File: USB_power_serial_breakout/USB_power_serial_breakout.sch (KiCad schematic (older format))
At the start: 18 parts, among them J1 Mount2, J2 Mount2, J3 USB_B, J4 UART, U1 FT230XS

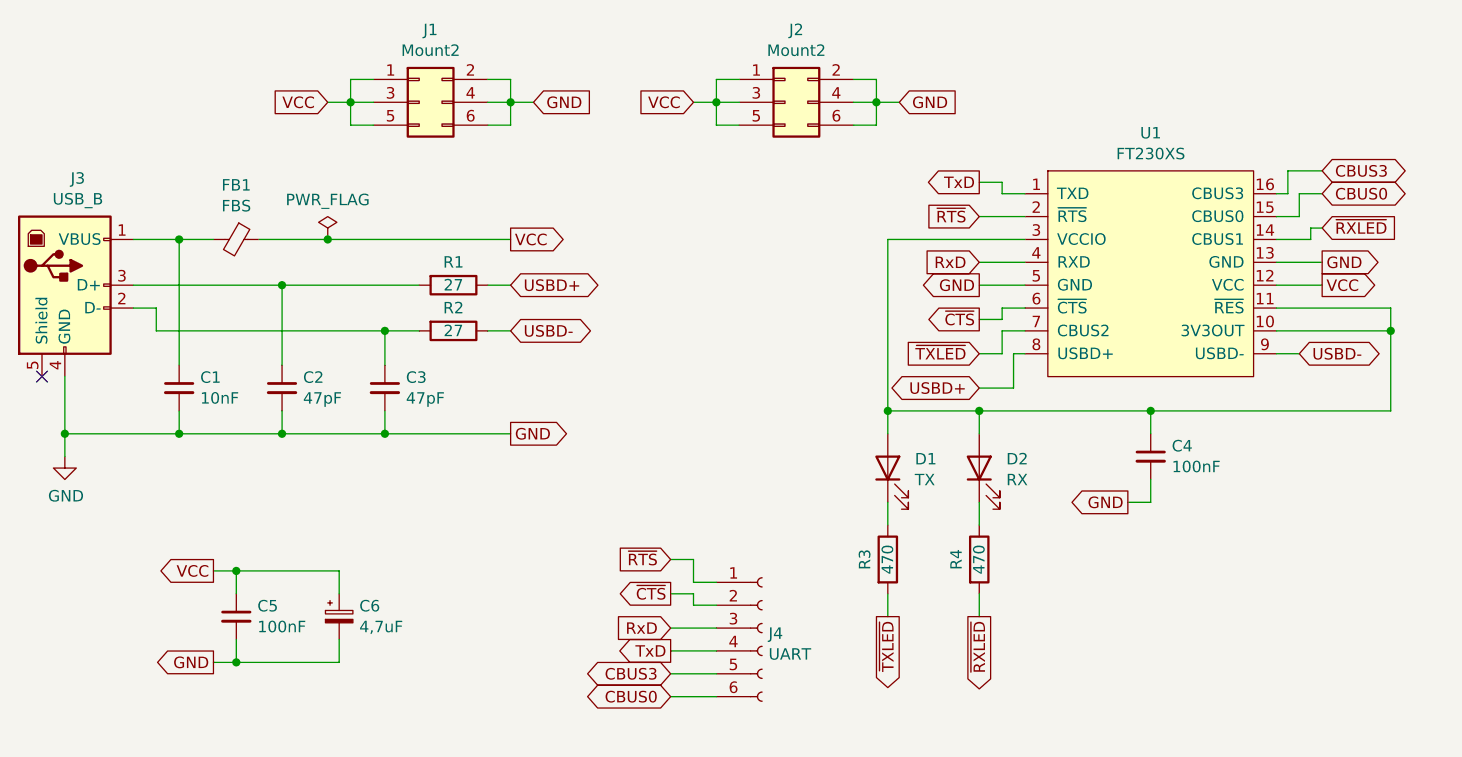
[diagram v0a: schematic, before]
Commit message: Updated the USB breakout board
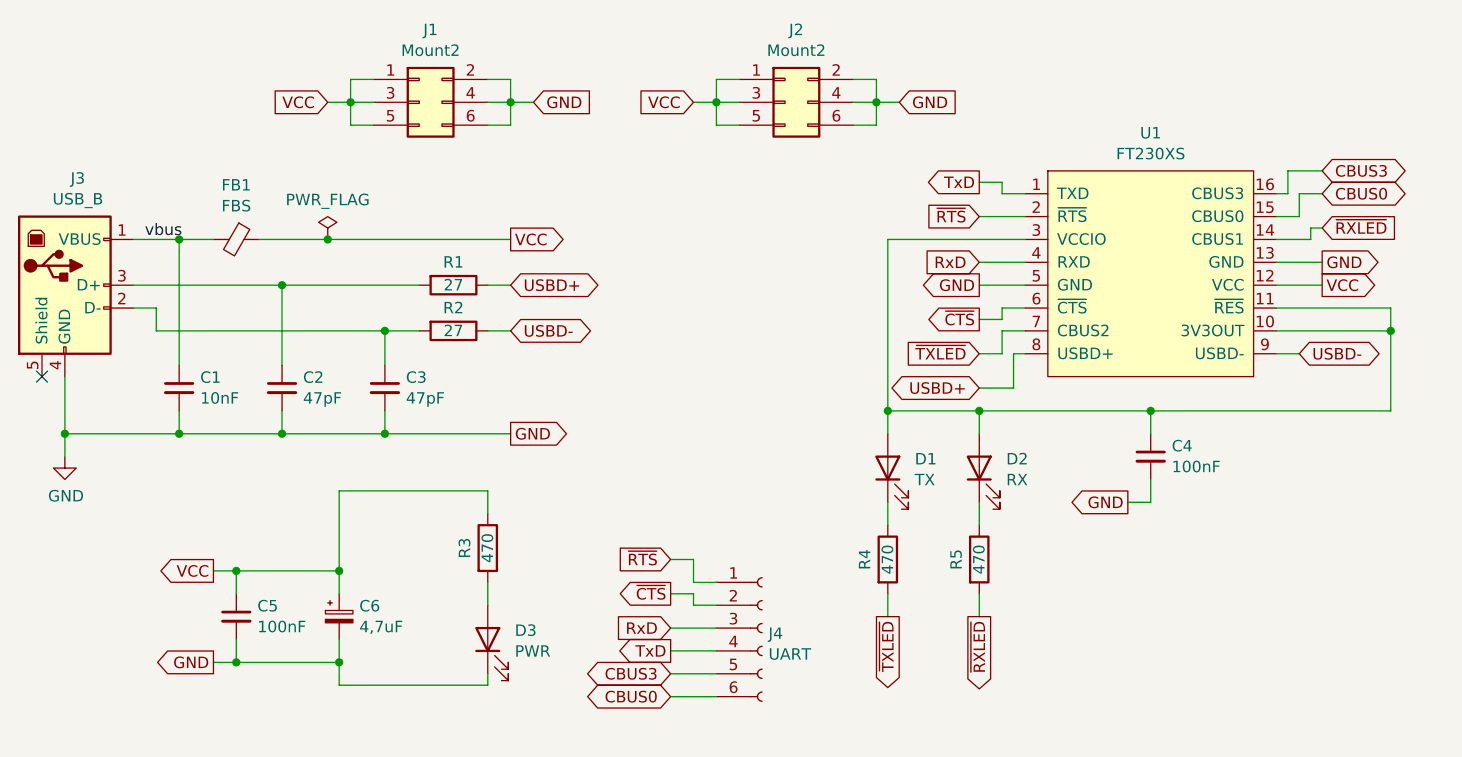
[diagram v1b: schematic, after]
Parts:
- added D3: PWR, LED_THT:LED_D3.0mm, symbol Device:LED
- added R3: 470, Resistor_SMD:R_1206_3216Metric_Pad1.30x1.75mm_HandSolder, symbol Device:R
- renumbered R3 to R4, R4 to R5
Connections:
- net GND: now also D3.1 (K)
- net VCC: now also R3.1
- net vbus: now reaches C1.1, FB1.2, J3.1 (VBUS)
- new net: D3.2 (A), R3.2
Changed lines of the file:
@@
 $EndComp
 $Comp
-L Device:R R3
+L Device:R R4
 U 1 1 609819CC
 P 6050 3350
-F 0 "R3" V 5950 3350 50  0000 C CNN
+F 0 "R4" V 5950 3350 50  0000 C CNN
 F 1 "470" V 6050 3350 50  0000 C CNN
 F 2 "Resistor_SMD:R_1206_3216Metric_Pad1.30x1.75mm_HandSolder" V 5980 3350 50  0001 C CNN
@@
 $EndComp
 $Comp
-L Device:R R4
+L Device:R R5
 U 1 1 60982650
 P 6450 3350
-F 0 "R4" V 6350 3350 50  0000 C CNN
+F 0 "R5" V 6350 3350 50  0000 C CNN
 F 1 "470" V 6450 3350 50  0000 C CNN
 F 2 "Resistor_SMD:R_1206_3216Metric_Pad1.30x1.75mm_HandSolder" V 6380 3350 50  0001 C CNN
@@
 Wire Wire Line
 	6000 1450 6000 1350
+$Comp
+L Device:R R3
+U 1 1 60968EC7
+P 4300 3300
+F 0 "R3" V 4200 3300 50  0000 C CNN
+F 1 "470" V 4300 3300 50  0000 C CNN
+F 2 "Resistor_SMD:R_1206_3216Metric_Pad1.30x1.75mm_HandSolder" V 4230 3300 50  0001 C CNN
+F 3 "~" H 4300 3300 50  0001 C CNN
+	1    4300 3300
+	1    0    0    -1
+$EndComp
+$Comp
+L Device:LED D3
+U 1 1 609693DC
+P 4300 3700
+F 0 "D3" V 4339 3582 50  0000 R CNN
+F 1 "PWR" V 4248 3582 50  0000 R CNN
+F 2 "LED_THT:LED_D3.0mm" H 4300 3700 50  0001 C CNN
+F 3 "~" H 4300 3700 50  0001 C CNN
+	1    4300 3700
+	0    -1   -1   0
+$EndComp
+Wire Wire Line
+	4300 3450 4300 3550
+Wire Wire Line
+	4300 3850 4300 3900
+Wire Wire Line
+	4300 3900 3650 3900
+Wire Wire Line
+	3650 3900 3650 3800
+Connection ~ 3650 3800
+Wire Wire Line
+	3650 3400 3650 3050
+Wire Wire Line
+	3650 3050 4300 3050
+Wire Wire Line
+	4300 3050 4300 3150
+Connection ~ 3650 3400
+Text Label 2800 1950 0    50   ~ 0
+vbus
 $EndSCHEMATC

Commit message: Updated USB/UART board
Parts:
- C6: footprint Capacitor_SMD:CP_Elec_4x5.8 -> Capacitor_THT:CP_Radial_D4.0mm_P2.00mm
- D1, D2, D3: footprint LED_THT:LED_D3.0mm -> LED_SMD:LED_1206_3216Metric_Pad1.42x1.75mm_HandSolder
- J4: footprint Connector_PinSocket_2.54mm:PinSocket_1x06_P2.54mm_Vertical -> Connector_PinSocket_2.54mm:PinSocket_1x08_P2.54mm_Vertical; symbol Connector:Conn_01x06_Female -> Connector:Conn_01x08_Female
- U1: footprint Package_SO:SSOP-16_5.3x6.2mm_P0.65mm -> Package_SO:SSOP-16_4.4x5.2mm_P0.65mm
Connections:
- net CBUS0: now also J4.8 (Pin_8); no longer J4.6 (Pin_6)
- net CBUS3: now also J4.7 (Pin_7); no longer J4.5 (Pin_5)
- net GND: now also J4.2 (Pin_2)
- net RxD: now also J4.5 (Pin_5); no longer J4.3 (Pin_3)
- net TxD: now also J4.6 (Pin_6); no longer J4.4 (Pin_4)
- net VCC: now also J4.1 (Pin_1)
- net ~CTS: now also J4.4 (Pin_4); no longer J4.2 (Pin_2)
- net ~RTS: now also J4.3 (Pin_3); no longer J4.1 (Pin_1)
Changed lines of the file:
@@
 F 0 "U1" H 7200 2715 50  0000 C CNN
 F 1 "FT230XS" H 7200 2624 50  0000 C CNN
-F 2 "Package_SO:SSOP-16_5.3x6.2mm_P0.65mm" H 7200 2600 50  0001 C CNN
+F 2 "Package_SO:SSOP-16_4.4x5.2mm_P0.65mm" H 7200 2600 50  0001 C CNN
 F 3 "" H 7200 2100 50  0001 C CNN
 	1    7200 2100
@@
 	7200 2700 8250 2700
 $Comp
-L Connector:Conn_01x06_Female J4
+L Connector:Conn_01x08_Female J4
 U 1 1 6096B972
-P 5500 3650
-F 0 "J4" H 5528 3626 50  0000 L CNN
-F 1 "UART" H 5528 3535 50  0000 L CNN
-F 2 "Connector_PinSocket_2.54mm:PinSocket_1x06_P2.54mm_Vertical" H 5500 3650 50  0001 C CNN
-F 3 "~" H 5500 3650 50  0001 C CNN
-	1    5500 3650
+P 5500 3550
+F 0 "J4" H 5528 3526 50  0000 L CNN
+F 1 "UART" H 5528 3435 50  0000 L CNN
+F 2 "Connector_PinSocket_2.54mm:PinSocket_1x08_P2.54mm_Vertical" H 5500 3550 50  0001 C CNN
+F 3 "~" H 5500 3550 50  0001 C CNN
+	1    5500 3550
 	1    0    0    -1
 $EndComp
@@
 Wire Wire Line
 	6550 2250 6650 2250
-Text GLabel 5100 3750 0    50   Output ~ 0
+Text GLabel 5000 3750 0    50   Output ~ 0
 TxD
-Text GLabel 5100 3650 0    50   Input ~ 0
+Text GLabel 5000 3650 0    50   Input ~ 0
 RxD
-Text GLabel 5100 3500 0    50   Output ~ 0
+Text GLabel 5000 3500 0    50   Output ~ 0
 ~CTS
-Text GLabel 5100 3350 0    50   Input ~ 0
+Text GLabel 5000 3350 0    50   Input ~ 0
 ~RTS
 Wire Wire Line
-	5100 3750 5300 3750
-Wire Wire Line
-	5100 3650 5300 3650
-Wire Wire Line
-	5100 3500 5200 3500
-Wire Wire Line
-	5200 3500 5200 3550
-Wire Wire Line
-	5200 3550 5300 3550
-Wire Wire Line
-	5100 3350 5200 3350
-Wire Wire Line
-	5200 3350 5200 3450
-Wire Wire Line
-	5200 3450 5300 3450
+	5000 3750 5300 3750
+Wire Wire Line
+	5000 3650 5300 3650
+Wire Wire Line
+	5000 3500 5100 3500
+Wire Wire Line
+	5100 3500 5100 3550
+Wire Wire Line
+	5100 3550 5300 3550
+Wire Wire Line
+	5000 3350 5100 3350
+Wire Wire Line
+	5100 3350 5100 3450
+Wire Wire Line
+	5100 3450 5300 3450
 $Comp
 L Device:C_Small C5
@@
 F 0 "C6" H 3738 3646 50  0000 L CNN
 F 1 "4,7uF" H 3738 3555 50  0000 L CNN
-F 2 "Capacitor_SMD:CP_Elec_4x5.8" H 3650 3600 50  0001 C CNN
+F 2 "Capacitor_THT:CP_Radial_D4.0mm_P2.00mm" H 3650 3600 50  0001 C CNN
 F 3 "~" H 3650 3600 50  0001 C CNN
 	1    3650 3600
@@
 F 0 "D1" V 6089 2832 50  0000 R CNN
 F 1 "TX" V 5998 2832 50  0000 R CNN
-F 2 "LED_THT:LED_D3.0mm" H 6050 2950 50  0001 C CNN
+F 2 "LED_SMD:LED_1206_3216Metric_Pad1.42x1.75mm_HandSolder" H 6050 2950 50  0001 C CNN
 F 3 "~" H 6050 2950 50  0001 C CNN
 	1    6050 2950
@@
 F 0 "D2" V 6489 2832 50  0000 R CNN
 F 1 "RX" V 6398 2832 50  0000 R CNN
-F 2 "LED_THT:LED_D3.0mm" H 6450 2950 50  0001 C CNN
+F 2 "LED_SMD:LED_1206_3216Metric_Pad1.42x1.75mm_HandSolder" H 6450 2950 50  0001 C CNN
 F 3 "~" H 6450 2950 50  0001 C CNN
 	1    6450 2950
@@
 Wire Wire Line
 	7950 2150 7750 2150
-Text GLabel 5100 3950 0    50   BiDi ~ 0
+Text GLabel 5000 3950 0    50   BiDi ~ 0
 CBUS0
-Text GLabel 5100 3850 0    50   BiDi ~ 0
+Text GLabel 5000 3850 0    50   BiDi ~ 0
 CBUS3
 Wire Wire Line
-	5100 3850 5300 3850
-Wire Wire Line
-	5100 3950 5300 3950
+	5000 3850 5300 3850
+Wire Wire Line
+	5000 3950 5300 3950
 $Comp
 L Connector_Generic:Conn_02x03_Odd_Even J1
@@
 F 0 "D3" V 4339 3582 50  0000 R CNN
 F 1 "PWR" V 4248 3582 50  0000 R CNN
-F 2 "LED_THT:LED_D3.0mm" H 4300 3700 50  0001 C CNN
+F 2 "LED_SMD:LED_1206_3216Metric_Pad1.42x1.75mm_HandSolder" H 4300 3700 50  0001 C CNN
 F 3 "~" H 4300 3700 50  0001 C CNN
 	1    4300 3700
@@
 Text Label 2800 1950 0    50   ~ 0
 vbus
+Text GLabel 5000 3200 0    50   Input ~ 0
+GND
+Text GLabel 5000 3100 0    50   Input ~ 0
+VCC
+Wire Wire Line
+	5000 3200 5150 3200
+Wire Wire Line
+	5150 3200 5150 3350
+Wire Wire Line
+	5150 3350 5300 3350
+Wire Wire Line
+	5000 3100 5200 3100
+Wire Wire Line
+	5200 3100 5200 3250
+Wire Wire Line
+	5200 3250 5300 3250
 $EndSCHEMATC
